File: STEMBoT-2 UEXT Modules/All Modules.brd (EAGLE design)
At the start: 160 x 100 mm, 132 parts, among them IC1 74HC165PW,118, IC2 74HC165PW,118, IC3 74HC165PW,118, J1 FTSH-105-01-XXX-DV-K, J2 FTSH-105-01-XXX-DV-K, J3 FTSH-105-01-XXX-DV-K, J4 FTSH-105-01-XXX-DV-K, J5 FTSH-105-01-XXX-DV-K, J6 FTSH-105-01-XXX-DV-K, Q1 MMBT3904LP-7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

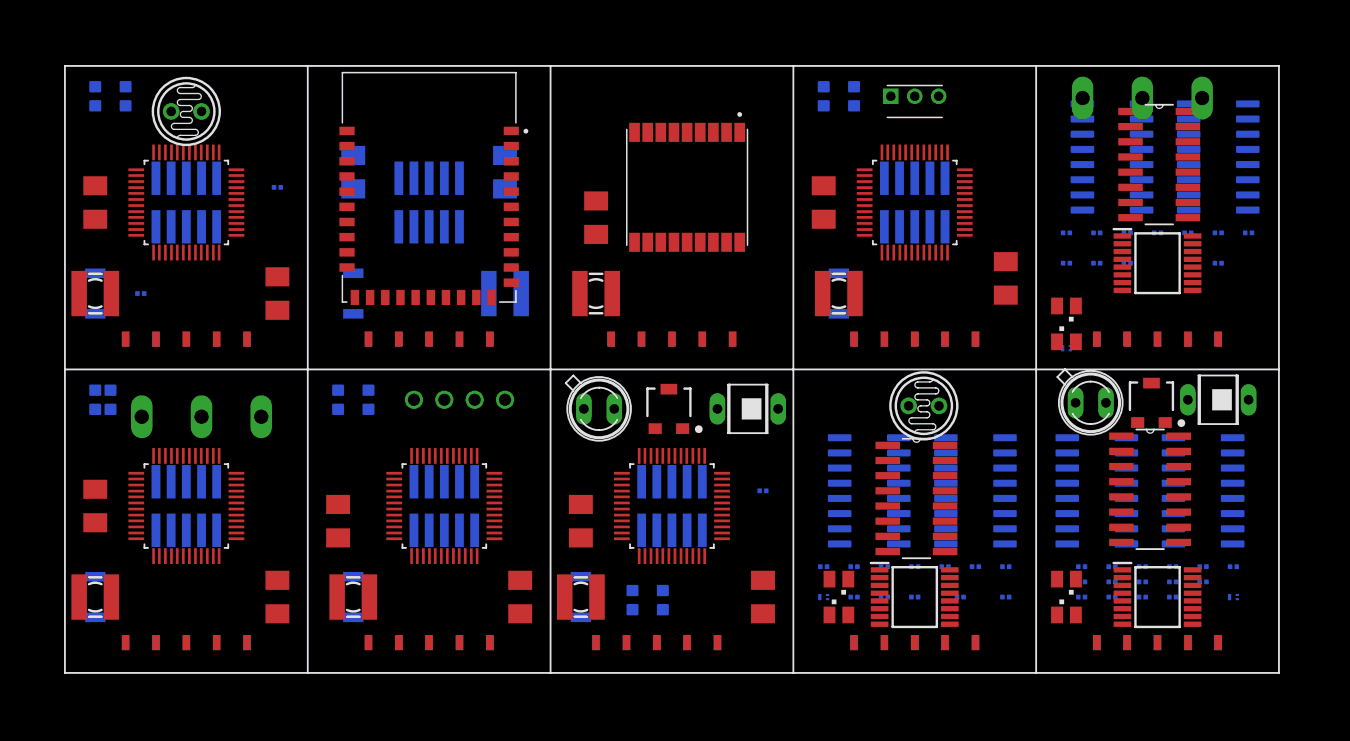
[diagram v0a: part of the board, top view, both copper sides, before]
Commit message: finish pcb traces
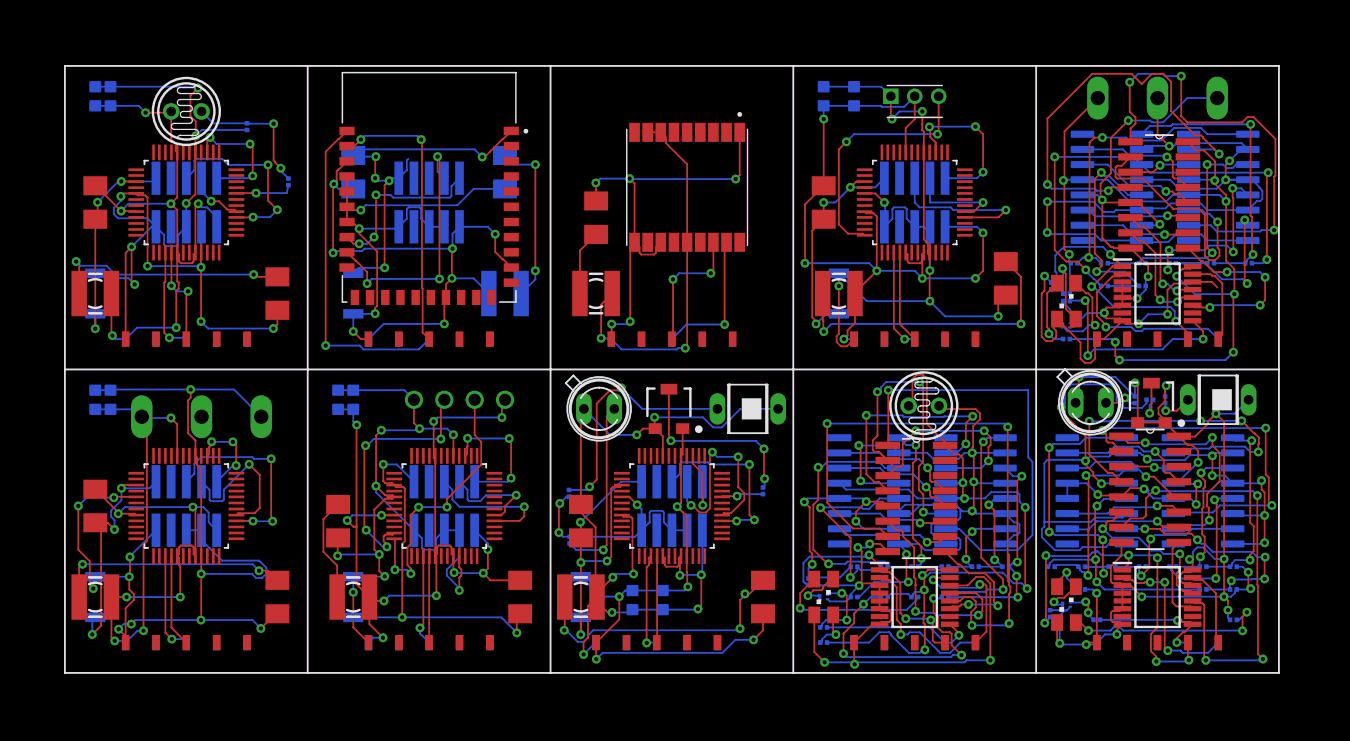
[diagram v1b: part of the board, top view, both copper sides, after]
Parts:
- added R56, R59, R60: ERJ-1RHD3601C, Resistor:RESC0603X26N
- moved R9 17.1 mm to (114.9, 48.3), turned to 270 degrees
- moved R10 17.1 mm to (117.5, 48.3), turned to 270 degrees
- moved R55 16.6 mm to (40.6, 71.1), turned to 270 degrees
- moved R14 14.1 mm to (116.2, 48.3)
- moved Q1 14.0 mm to (109.2, 31.1)
- moved R29 13.0 mm to (124.5, 59.7)
- moved R13 9.94 mm to (111.8, 29.8), turned to 180 degrees
- moved R1 9.53 mm to (112.4, 59.7)
- moved R24 9.25 mm to (115.6, 59.7), turned to 180 degrees
- moved R30 8.89 mm to (109.2, 53.3), turned to 180 degrees
- moved R4 8.03 mm to (88.9, 29.2)
- moved R23 6.35 mm to (88.9, 27.9)
- moved R27 6.29 mm to (112.4, 57.8), turned to 180 degrees
- moved R12 5.43 mm to (123.2, 29.8)
- moved R37 5.12 mm to (120.7, 32.4)
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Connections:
- removed net N$145: IC2.1, U$2.8
- removed net N$159: R61.1
- removed net N$163: IC3.1, U$1.8
- removed net N$2: U1.3
- new net N$158: IC3.1, R56.1, U$1.8
- new net N$164: IC2.1, R60.1, U$2.8
- net N$100: now also U4.13; no longer U4.1
- net N$125: now also U1.3
- net N$157: now also R61.1
- net N$162: now also R59.1
- net N$20: no longer IC1.10
- net N$39: now also IC1.14, IC1.3, IC1.4, IC1.5, IC1.6, R59.2
- net N$43: now also U7.1; no longer U7.13
- net N$44: now also U7.13; no longer U7.1
- net N$53: no longer IC2.10
- net N$55: now also R56.2
- net N$64: now also IC2.14, IC2.3, IC2.4, IC2.5, IC2.6, R60.2
- net N$68: now also U10.1; no longer U10.13
- net N$69: now also U10.13; no longer U10.1
- net N$99: now also U4.1; no longer U4.13
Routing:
- net N$55: track 0.00 -> 119.4 mm, vias 0 -> 20
- net N$144: track 0.00 -> 91.9 mm, vias 0 -> 11
- net N$161: track 0.00 -> 83.5 mm, vias 0 -> 10
- net N$39: track 0.00 -> 79.3 mm, vias 0 -> 10
- net N$64: track 0.00 -> 77.7 mm, vias 0 -> 9
- net N$108: track 0.00 -> 77.3 mm, vias 0 -> 9
- net N$138: track 0.00 -> 76.5 mm, vias 0 -> 9
- net N$79: track 0.00 -> 75.1 mm, vias 0 -> 9
- net N$12: track 0.00 -> 74.5 mm, vias 0 -> 7
- net N$51: track 0.00 -> 73.8 mm, vias 0 -> 7
- net N$109: track 0.00 -> 70.7 mm, vias 0 -> 5
- net N$113: track 0.00 -> 70.4 mm, vias 0 -> 11
- net N$137: track 0.00 -> 69.2 mm, vias 0 -> 8
- net N$119: track 0.00 -> 67.4 mm, vias 0 -> 7
- net N$1: track 0.00 -> 66.0 mm, vias 0 -> 9
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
